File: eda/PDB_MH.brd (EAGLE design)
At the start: 101.6 x 81.3 mm, 18 parts

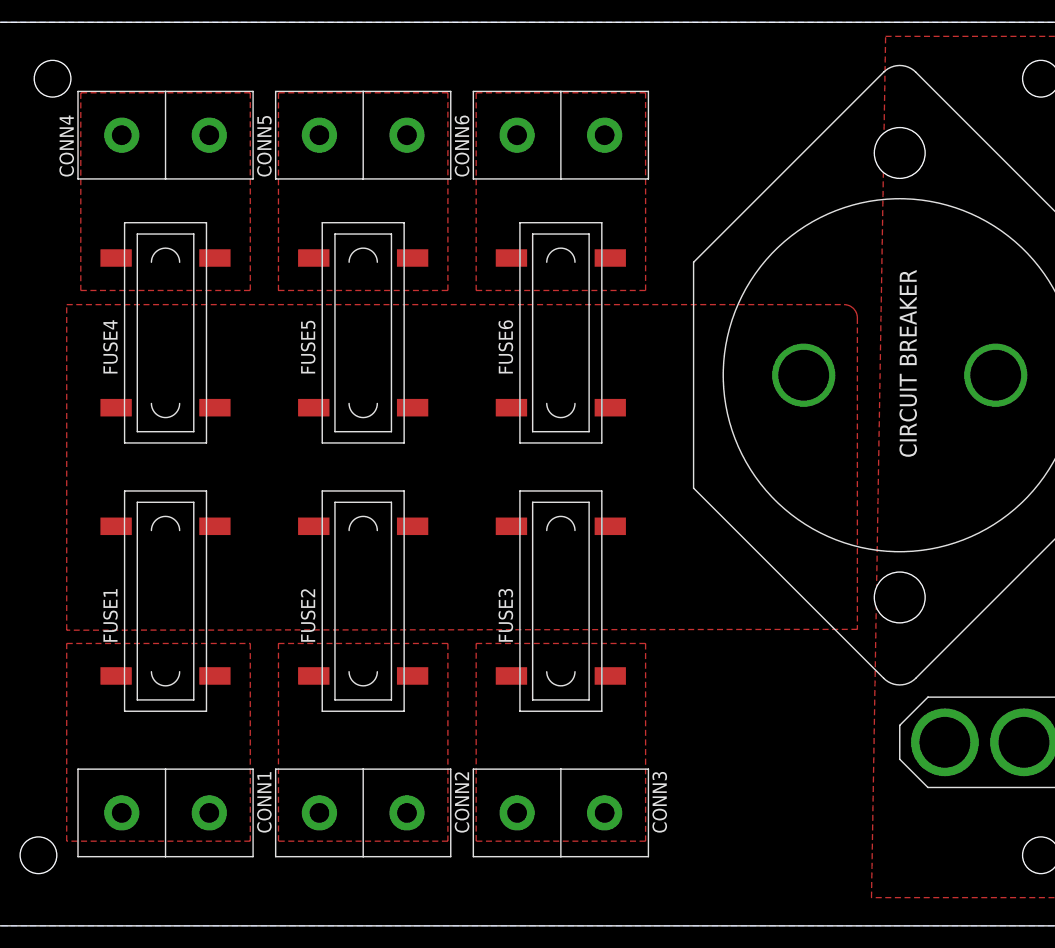
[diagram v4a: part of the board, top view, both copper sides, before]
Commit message: Added Copyright and logo
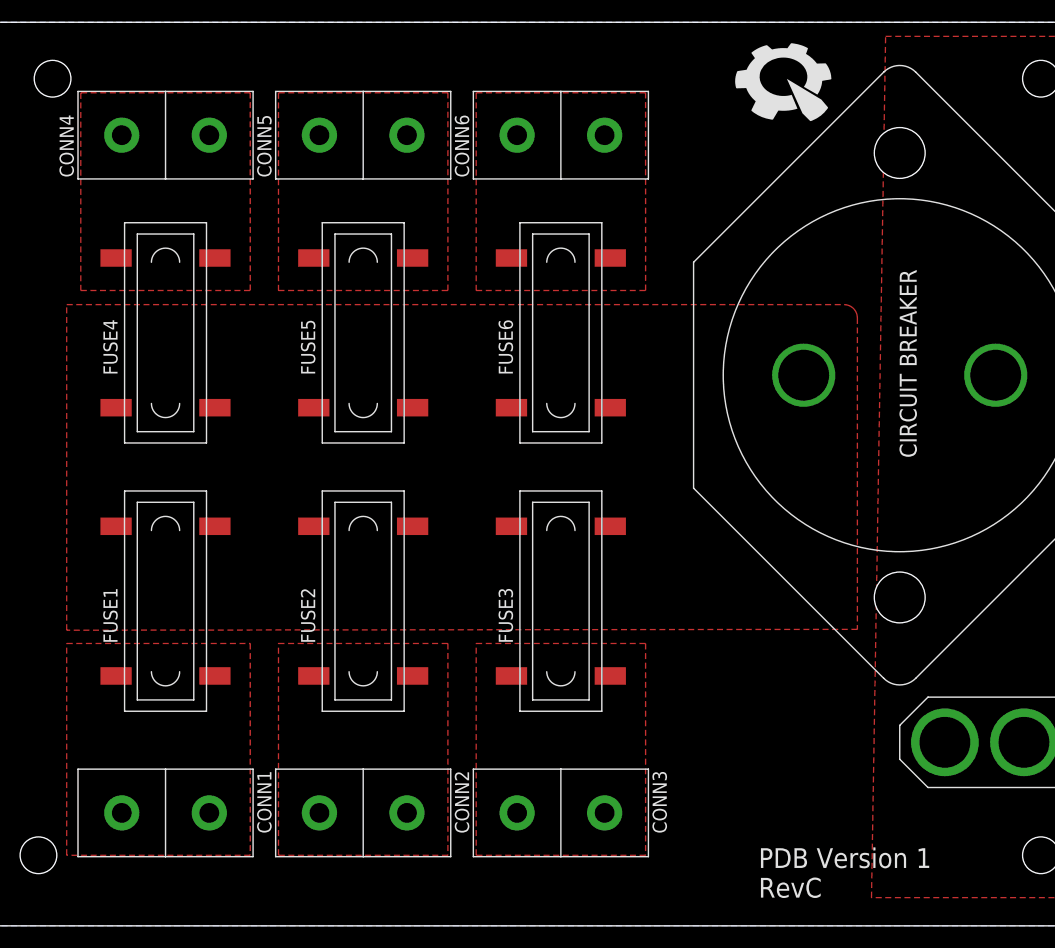
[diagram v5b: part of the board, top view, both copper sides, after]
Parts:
- added U$6: (no value), pie:PIE-LOGO-SMALL
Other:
- board text added: "Copyright (c) 2013, Pioneers in Engineering All rights reserved. Design by: Sharabesh R, Mohammed H, Tobin H. This design is open source hardware. For more information, visit pioneers.berkeley.edu/opensource"
- board text added: "PDB Version 1 RevC"
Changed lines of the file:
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@@
 <wire x1="101.6" y1="81.28" x2="0" y2="81.28" width="0" layer="20"/>
 <wire x1="0" y1="81.28" x2="0" y2="0" width="0" layer="20"/>
+<text x="63.5" y="34.29" size="1.524" layer="22" font="vector" rot="MR0">Copyright (c) 2013, Pioneers in Engineering
+All rights reserved.
+Design by: Sharabesh R, Mohammed H, Tobin H.
+This design is open source hardware.
+For more information, visit
+pioneers.berkeley.edu/opensource</text>
+<text x="69.85" y="2.54" size="1.778" layer="21" font="vector">PDB Version 1
+RevC</text>
 </plain>
 <attributes>
@@
 <element name="U$4" library="pie" package="STAND-OFF" value="" x="95.25" y="76.2" rot="R90"/>
 <element name="U$5" library="pie" package="STAND-OFF" value="" x="95.25" y="6.35"/>
+<element name="U$6" library="pie" package="PIE-LOGO-SMALL" value="" x="72.39" y="76.2"/>
 </elements>
 <signals>
@@
 <vertex x="26.67" y="25.4"/>
 <vertex x="41.91" y="25.4"/>
-<vertex x="41.91" y="7.62"/>
-<vertex x="26.67" y="7.62"/>
+<vertex x="41.91" y="6.35"/>
+<vertex x="26.67" y="6.35"/>
 </polygon>
 </signal>
@@
 <vertex x="7.62" y="25.4"/>
 <vertex x="24.13" y="25.4"/>
-<vertex x="24.13" y="7.62"/>
-<vertex x="7.62" y="7.62"/>
+<vertex x="24.13" y="6.35"/>
+<vertex x="7.62" y="6.35"/>
 </polygon>
 </signal>
@@
 <vertex x="44.45" y="25.4"/>
 <vertex x="59.69" y="25.4"/>
-<vertex x="59.69" y="7.62"/>
-<vertex x="44.45" y="7.62"/>
+<vertex x="59.69" y="6.35"/>
+<vertex x="44.45" y="6.35"/>
 </polygon>
 </signal>
@@
 </board>
 </drawing>
+<compatibility>
+<note version="6.3" minversion="6.2.2" severity="warning">
+Since Version 6.2.2 text objects can contain more than one line,
+which will not be processed correctly with this version.
+</note>
+</compatibility>
 </eagle>

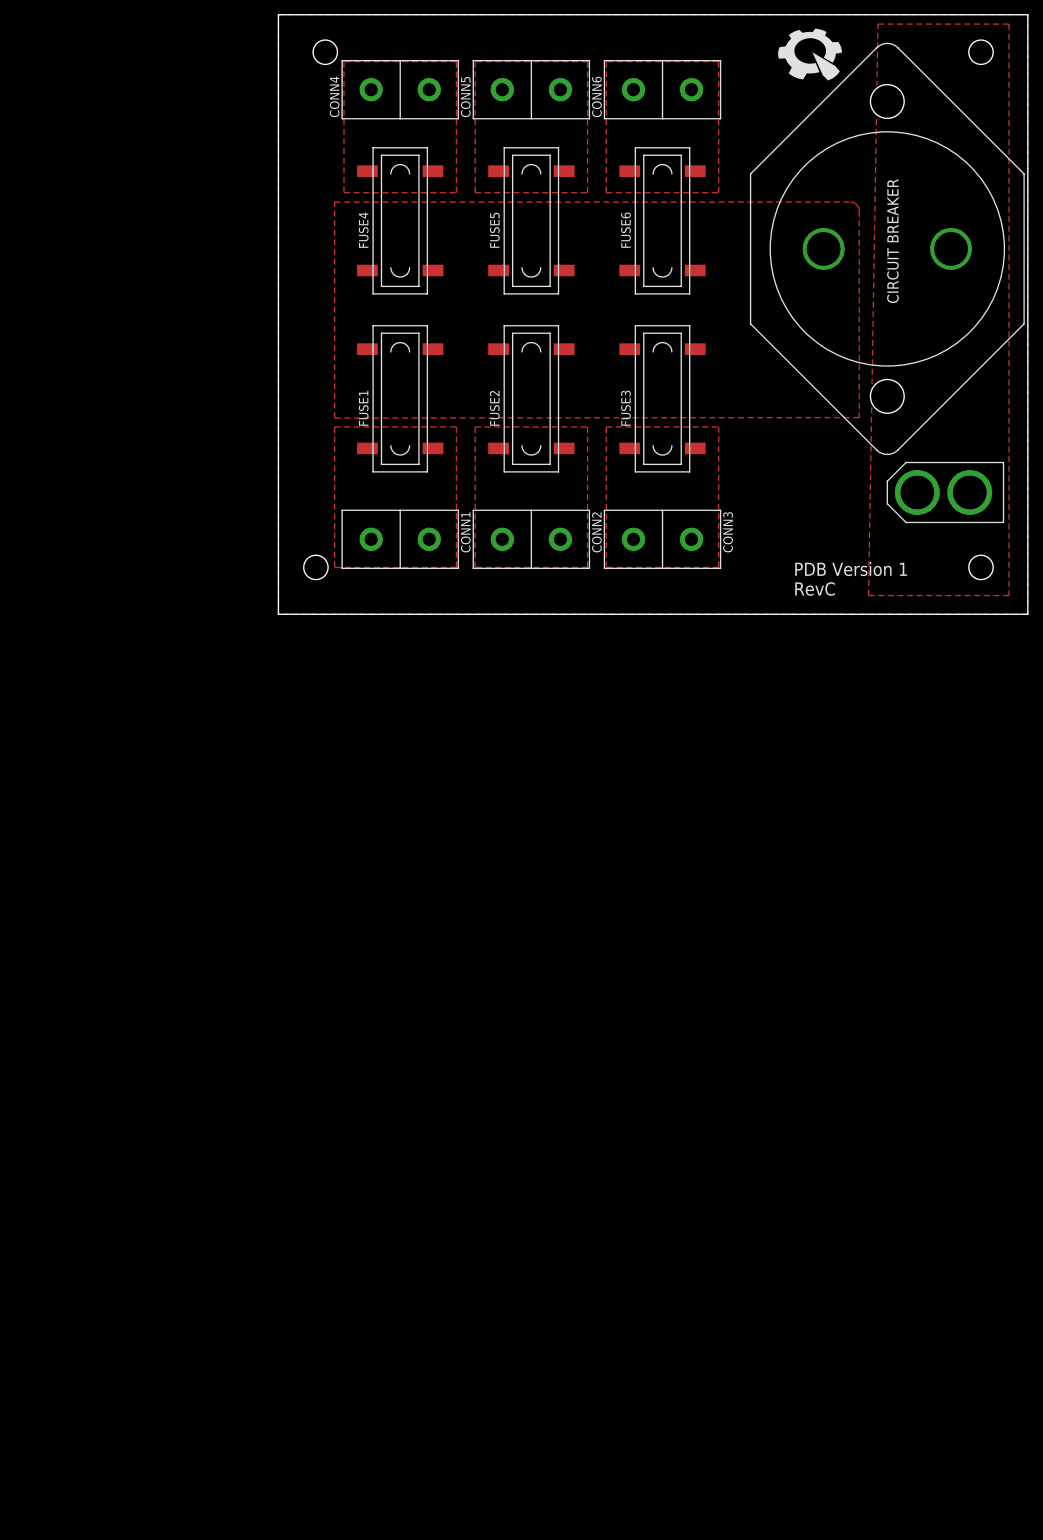
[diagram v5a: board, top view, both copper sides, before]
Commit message: Added 4 Anderson Connectors and Buck Converter to Schematic
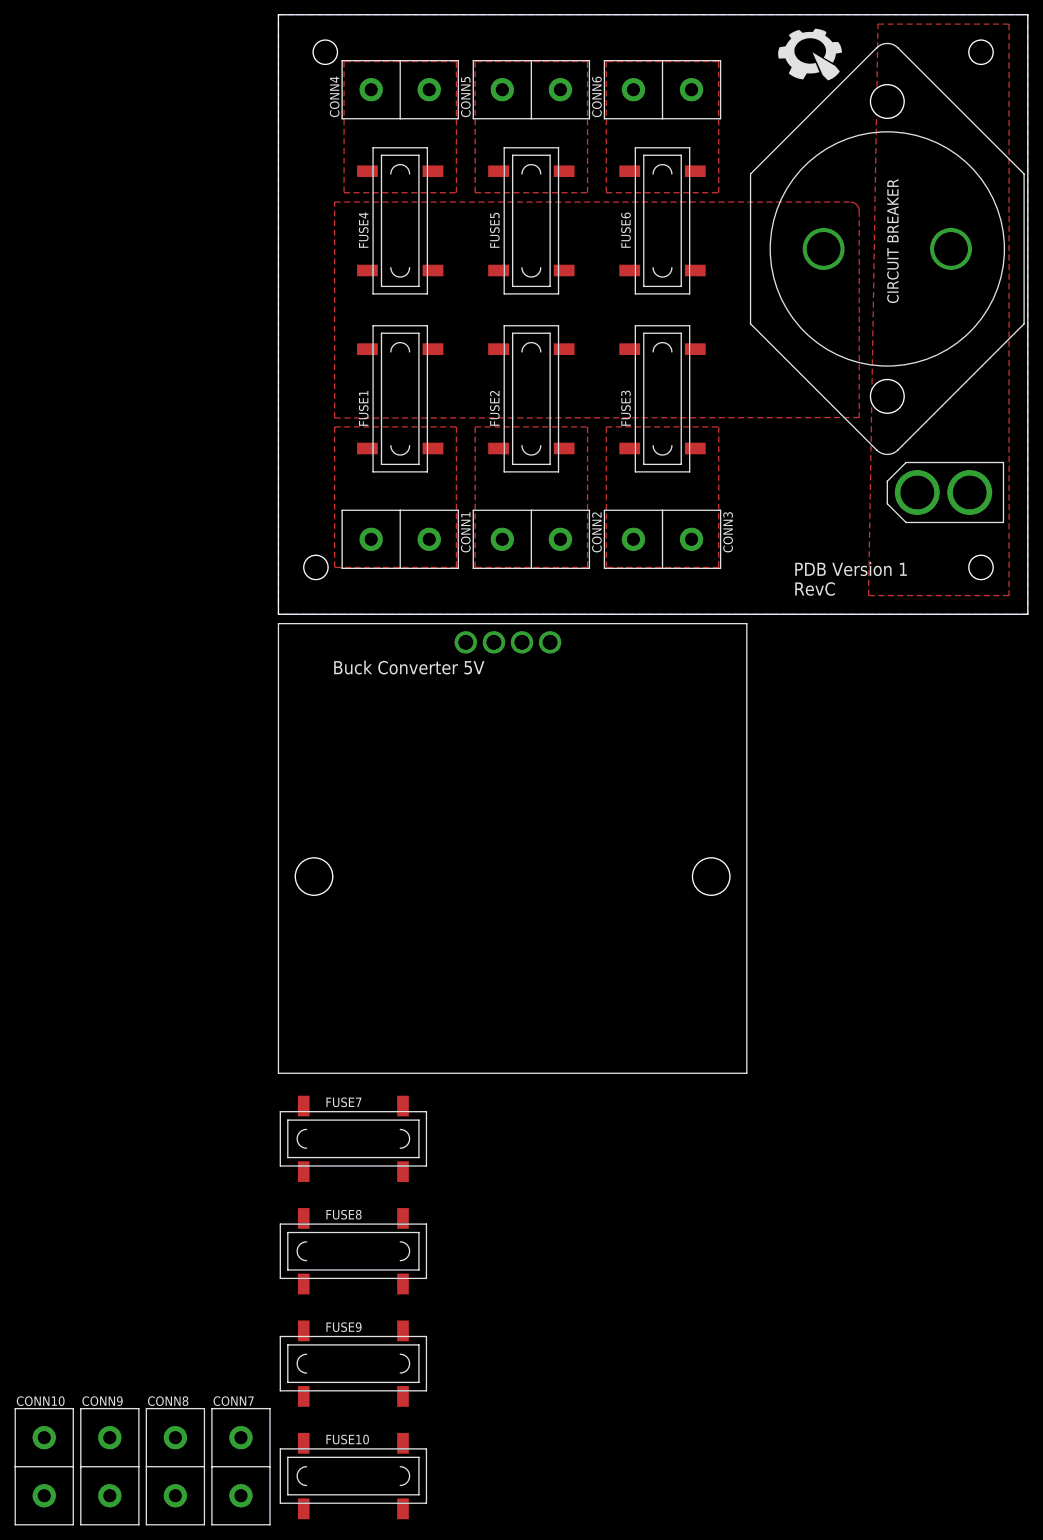
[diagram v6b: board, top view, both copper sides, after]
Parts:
- added CONN10, CONN7, CONN8, CONN9: ANDERSONVERTICAL, pie:ANDERSON_VERTICAL
- added FUSE10, FUSE7, FUSE8, FUSE9: FUSE_HOLDER_SMD, pie:FUSE_HOLDER_SMD
- added U$7: BUCK_CONVERTER_5V, pie:BUCK_CONVERTER_5V
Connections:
- new net N$1: FUSE10.P$2_DOWN, FUSE10.P$2_UP, FUSE7.P$1_DOWN, FUSE7.P$1_UP, FUSE8.P$2_DOWN, FUSE8.P$2_UP, FUSE9.P$1_DOWN, FUSE9.P$1_UP, U$7.P$6
- new net N$2: CONN7.PIN2, FUSE7.P$2_DOWN, FUSE7.P$2_UP
- new net N$3: CONN10.PIN2, FUSE8.P$1_DOWN, FUSE8.P$1_UP
- new net N$4: CONN9.PIN2, FUSE10.P$1_DOWN, FUSE10.P$1_UP
- new net N$5: CONN8.PIN2, FUSE9.P$2_DOWN, FUSE9.P$2_UP
- net BAT: now also U$7.P$4
- net GND: now also CONN10.PIN1, CONN7.PIN1, CONN8.PIN1, CONN9.PIN1, U$7.P$3, U$7.P$5
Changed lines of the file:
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@@
 <layers>
 <layer number="1" name="Top" color="4" fill="1" visible="yes" active="yes"/>
+<layer number="2" name="Route2" color="1" fill="3" visible="no" active="no"/>
+<layer number="3" name="Route3" color="4" fill="3" visible="no" active="no"/>
+<layer number="14" name="Route14" color="1" fill="6" visible="no" active="no"/>
+<layer number="15" name="Route15" color="4" fill="6" visible="no" active="no"/>
 <layer number="16" name="Bottom" color="1" fill="1" visible="yes" active="yes"/>
 <layer number="17" name="Pads" color="2" fill="1" visible="yes" active="yes"/>
@@
 <element name="U$5" library="pie" package="STAND-OFF" value="" x="95.25" y="6.35"/>
 <element name="U$6" library="pie" package="PIE-LOGO-SMALL" value="" x="72.39" y="76.2"/>
+<element name="U$7" library="pie" package="BUCK_CONVERTER_5V" value="BUCK_CONVERTER_5V" x="31.75" y="-35.56"/>
+<element name="FUSE7" library="pie" package="FUSE_HOLDER_SMD" value="FUSE_HOLDER_SMD" x="10.16" y="-71.12">
+<attribute name="MANUF-PN" value="3587" x="10.16" y="-71.12" size="1.778" layer="27" display="off"/>
+<attribute name="MANUF" value="KEYSTONE" x="10.16" y="-71.12" size="1.778" layer="27" display="off"/>
+<attribute name="DIGIKEY-PN" value=" 36-3587-ND" x="10.16" y="-71.12" size="1.778" layer="27" display="off"/>
+</element>
+<element name="FUSE8" library="pie" package="FUSE_HOLDER_SMD" value="FUSE_HOLDER_SMD" x="10.16" y="-86.36">
+<attribute name="MANUF-PN" value="3587" x="10.16" y="-86.36" size="1.778" layer="27" display="off"/>
+<attribute name="MANUF" value="KEYSTONE" x="10.16" y="-86.36" size="1.778" layer="27" display="off"/>
+<attribute name="DIGIKEY-PN" value=" 36-3587-ND" x="10.16" y="-86.36" size="1.778" layer="27" display="off"/>
+</element>
+<element name="FUSE9" library="pie" package="FUSE_HOLDER_SMD" value="FUSE_HOLDER_SMD" x="10.16" y="-101.6">
+<attribute name="MANUF-PN" value="3587" x="10.16" y="-101.6" size="1.778" layer="27" display="off"/>
+<attribute name="MANUF" value="KEYSTONE" x="10.16" y="-101.6" size="1.778" layer="27" display="off"/>
+<attribute name="DIGIKEY-PN" value=" 36-3587-ND" x="10.16" y="-101.6" size="1.778" layer="27" display="off"/>
+</element>
+<element name="FUSE10" library="pie" package="FUSE_HOLDER_SMD" value="FUSE_HOLDER_SMD" x="10.16" y="-116.84">
+<attribute name="MANUF-PN" value="3587" x="10.16" y="-116.84" size="1.778" layer="27" display="off"/>
+<attribute name="MANUF" value="KEYSTONE" x="10.16" y="-116.84" size="1.778" layer="27" display="off"/>
+<attribute name="DIGIKEY-PN" value=" 36-3587-ND" x="10.16" y="-116.84" size="1.778" layer="27" display="off"/>
+</element>
+<element name="CONN7" library="pie" package="ANDERSON_VERTICAL" value="ANDERSONVERTICAL" x="-5.08" y="-115.57">
+<attribute name="PIE-INT-REF-NUM" value="Anderson" x="-5.08" y="-115.57" size="1.778" layer="27" display="off"/>
+</element>
+<element name="CONN8" library="pie" package="ANDERSON_VERTICAL" value="ANDERSONVERTICAL" x="-13.97" y="-115.57">
+<attribute name="PIE-INT-REF-NUM" value="Anderson" x="-13.97" y="-115.57" size="1.778" layer="27" display="off"/>
+</element>
+<element name="CONN9" library="pie" package="ANDERSON_VERTICAL" value="ANDERSONVERTICAL" x="-22.86" y="-115.57">
+<attribute name="PIE-INT-REF-NUM" value="Anderson" x="-22.86" y="-115.57" size="1.778" layer="27" display="off"/>
+</element>
+<element name="CONN10" library="pie" package="ANDERSON_VERTICAL" value="ANDERSONVERTICAL" x="-31.75" y="-115.57">
+<attribute name="PIE-INT-REF-NUM" value="Anderson" x="-31.75" y="-115.57" size="1.778" layer="27" display="off"/>
+</element>
 </elements>
 <signals>
@@
 <contactref element="CONN5" pad="PIN1"/>
 <contactref element="CONN6" pad="PIN1"/>
+<contactref element="CONN9" pad="PIN1"/>
+<contactref element="CONN10" pad="PIN1"/>
+<contactref element="CONN7" pad="PIN1"/>
+<contactref element="CONN8" pad="PIN1"/>
+<contactref element="U$7" pad="P$3"/>
+<contactref element="U$7" pad="P$5"/>
+<wire x1="-22.86" y1="-119.507" x2="-31.75" y2="-119.507" width="0" layer="19" extent="1-1"/>
+<wire x1="-13.97" y1="-119.507" x2="-22.86" y2="-119.507" width="0" layer="19" extent="1-1"/>
+<wire x1="-5.08" y1="-119.507" x2="-13.97" y2="-119.507" width="0" layer="19" extent="1-1"/>
+<wire x1="29.21" y1="-3.81" x2="-5.08" y2="-119.507" width="0" layer="19" extent="1-1"/>
+<wire x1="33.02" y1="-3.81" x2="29.21" y2="-3.81" width="0" layer="19" extent="1-1"/>
+<wire x1="30.353" y1="10.16" x2="29.21" y2="-3.81" width="0" layer="19" extent="1-1"/>
+<wire x1="48.133" y1="10.16" x2="30.353" y2="10.16" width="0" layer="19" extent="1-1"/>
+<wire x1="12.573" y1="10.16" x2="30.353" y2="10.16" width="0" layer="19" extent="1-1"/>
+<wire x1="86.614" y1="16.51" x2="48.133" y2="10.16" width="0" layer="19" extent="1-1"/>
+<wire x1="56.007" y1="71.12" x2="48.133" y2="10.16" width="0" layer="19" extent="1-1"/>
+<wire x1="38.227" y1="71.12" x2="56.007" y2="71.12" width="0" layer="19" extent="1-1"/>
+<wire x1="20.447" y1="71.12" x2="38.227" y2="71.12" width="0" layer="19" extent="1-1"/>
 </signal>
 <signal name="VOUT2">
@@
 <vertex x="80.01" y="2.54"/>
 </polygon>
+<contactref element="U$7" pad="P$4"/>
+<wire x1="93.726" y1="16.51" x2="91.186" y2="49.53" width="0" layer="19" extent="1-1"/>
+<wire x1="36.83" y1="-3.81" x2="93.726" y2="16.51" width="0" layer="19" extent="1-1"/>
 </signal>
 <signal name="VOUT6">
@@
 </polygon>
 </signal>
+<signal name="N$1">
+<contactref element="U$7" pad="P$6"/>
+<contactref element="FUSE10" pad="P$2_DOWN"/>
+<contactref element="FUSE10" pad="P$2_UP"/>
+<contactref element="FUSE9" pad="P$1_UP"/>
+<contactref element="FUSE9" pad="P$1_DOWN"/>
+<contactref element="FUSE8" pad="P$2_DOWN"/>
+<contactref element="FUSE8" pad="P$2_UP"/>
+<contactref element="FUSE7" pad="P$1_UP"/>
+<contactref element="FUSE7" pad="P$1_DOWN"/>
+<wire x1="16.891" y1="-112.395" x2="16.891" y2="-121.285" width="0" layer="19" extent="1-1"/>
+<wire x1="3.429" y1="-106.045" x2="16.891" y2="-112.395" width="0" layer="19" extent="1-1"/>
+<wire x1="3.429" y1="-97.155" x2="3.429" y2="-106.045" width="0" layer="19" extent="1-1"/>
+<wire x1="16.891" y1="-90.805" x2="3.429" y2="-97.155" width="0" layer="19" extent="1-1"/>
+<wire x1="16.891" y1="-81.915" x2="16.891" y2="-90.805" width="0" layer="19" extent="1-1"/>
+<wire x1="3.429" y1="-75.565" x2="16.891" y2="-81.915" width="0" layer="19" extent="1-1"/>
+<wire x1="3.429" y1="-66.675" x2="3.429" y2="-75.565" width="0" layer="19" extent="1-1"/>
+<wire x1="25.4" y1="-3.81" x2="3.429" y2="-66.675" width="0" layer="19" extent="1-1"/>
+</signal>
+<signal name="N$2">
+<contactref element="FUSE7" pad="P$2_DOWN"/>
+<contactref element="FUSE7" pad="P$2_UP"/>
+<contactref element="CONN7" pad="PIN2"/>
+<wire x1="16.891" y1="-75.565" x2="-5.08" y2="-111.633" width="0" layer="19" extent="1-1"/>
+<wire x1="16.891" y1="-66.675" x2="16.891" y2="-75.565" width="0" layer="19" extent="1-1"/>
+</signal>
+<signal name="N$3">
+<contactref element="FUSE8" pad="P$1_UP"/>
+<contactref element="FUSE8" pad="P$1_DOWN"/>
+<contactref element="CONN10" pad="PIN2"/>
+<wire x1="3.429" y1="-90.805" x2="-31.75" y2="-111.633" width="0" layer="19" extent="1-1"/>
+<wire x1="3.429" y1="-81.915" x2="3.429" y2="-90.805" width="0" layer="19" extent="1-1"/>
+</signal>
+<signal name="N$5">
+<contactref element="FUSE9" pad="P$2_DOWN"/>
+<contactref element="FUSE9" pad="P$2_UP"/>
+<contactref element="CONN8" pad="PIN2"/>
+<wire x1="16.891" y1="-106.045" x2="-13.97" y2="-111.633" width="0" layer="19" extent="1-1"/>
+<wire x1="16.891" y1="-97.155" x2="16.891" y2="-106.045" width="0" layer="19" extent="1-1"/>
+</signal>
+<signal name="N$4">
+<contactref element="FUSE10" pad="P$1_UP"/>
+<contactref element="FUSE10" pad="P$1_DOWN"/>
+<contactref element="CONN9" pad="PIN2"/>
+<wire x1="3.429" y1="-112.395" x2="-22.86" y2="-111.633" width="0" layer="19" extent="1-1"/>
+<wire x1="3.429" y1="-121.285" x2="3.429" y2="-112.395" width="0" layer="19" extent="1-1"/>
+</signal>
 </signals>
